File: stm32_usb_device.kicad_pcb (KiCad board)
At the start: 2 copper layers, 0 parts

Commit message: schematic: Add power supply, decoupling caps, pin headers
Signed-off-by: Tomislav Milkovic <tomislav.milkovic95@gmail.com>
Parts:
- added C1: 10u, Capacitor_SMD:C_0603_1608Metric, F.Cu at (94.2, 91.5)
- added C10: 10u, Capacitor_SMD:C_0603_1608Metric, F.Cu at (105.7, 80.9)
- added C11: 100n, Capacitor_SMD:C_0402_1005Metric, F.Cu at (118.6, 80.8)
- added C12: 100n, Capacitor_SMD:C_0402_1005Metric, F.Cu at (118.6, 94.7)
- added C2: 10u, Capacitor_SMD:C_0603_1608Metric, F.Cu at (102.1, 90.3)
- added C3: 10p, Capacitor_SMD:C_0402_1005Metric, F.Cu at (117.7, 88.3)
- added C4: 10p, Capacitor_SMD:C_0402_1005Metric, F.Cu at (117.6, 86.3)
- added C5: 100n, Capacitor_SMD:C_0402_1005Metric, F.Cu at (117.2, 84.1)
- added C6: 100n, Capacitor_SMD:C_0402_1005Metric, F.Cu at (106.1, 82.4)
- added C7: 100n, Capacitor_SMD:C_0402_1005Metric, F.Cu at (116.3, 90.9)
- added C8: 100n, Capacitor_SMD:C_0402_1005Metric, F.Cu at (114.1, 92.8)
- added C9: 100n, Capacitor_SMD:C_0402_1005Metric, F.Cu at (105.8, 91.5)
- added D1: PWR_LED_R, LED_SMD:LED_0603_1608Metric, F.Cu at (100.2, 96.8)
- added D2: USR_LED_R, LED_SMD:LED_0603_1608Metric, F.Cu at (132.0, 81.0)
- added FB1: 100R@100 MHz, Inductor_SMD:L_0805_2012Metric, F.Cu at (91.2, 90.6)
- added J1: USB_A, Connector_USB:USB_A_CNCTech_1001-011-01101_Horizontal, F.Cu at (81.9, 87.5)
- added J2: Conn_01x05, Connector_PinHeader_2.54mm:PinHeader_1x05_P2.54mm_Vertical, F.Cu at (105.4, 97.7)
- added J3: Conn_01x03, Connector_PinHeader_2.54mm:PinHeader_1x03_P2.54mm_Vertical, F.Cu at (107.2, 74.7)
- added R1: 1k5, Resistor_SMD:R_0402_1005Metric, F.Cu at (97.1, 96.7)
- added R2: 1k5, Resistor_SMD:R_0402_1005Metric, F.Cu at (132.0, 84.1)
- added R3: 1k5, Resistor_SMD:R_0402_1005Metric, F.Cu at (111.8, 94.4)
- added R4: 1k5, Resistor_SMD:R_0402_1005Metric, F.Cu at (115.9, 80.2)
- added R5: 1k5, Resistor_SMD:R_0402_1005Metric, F.Cu at (129.4, 78.5)
- added R6: 1k5, Resistor_SMD:R_0402_1005Metric, F.Cu at (94.6, 85.4)
- added R7: 1k5, Resistor_SMD:R_0402_1005Metric, F.Cu at (129.1, 97.3)
- added SW1: RST_SW, Button_Switch_SMD:SW_SPST_CK_RS282G05A3, F.Cu at (124.2, 81.6)
- added SW2: USR_SW, Button_Switch_SMD:SW_SPST_CK_RS282G05A3, F.Cu at (124.2, 94.2)
- added TP1: TestPoint_Small, TestPoint:TestPoint_Pad_D1.0mm, F.Cu at (103.6, 78.3)
- added TP10: TestPoint_Small, TestPoint:TestPoint_Pad_D1.0mm, F.Cu at (103.0, 101.8)
- added TP11: TestPoint_Small, TestPoint:TestPoint_Pad_D1.0mm, F.Cu at (111.0, 102.4)
- added TP12: TestPoint_Small, TestPoint:TestPoint_Pad_D1.0mm, F.Cu at (116.4, 102.7)
- added TP2: TestPoint_Small, TestPoint:TestPoint_Pad_D1.0mm, F.Cu at (112.8, 78.4)
- added TP3: TestPoint_Small, TestPoint:TestPoint_Pad_D1.0mm, F.Cu at (109.6, 78.4)
- added TP4: TestPoint_Small, TestPoint:TestPoint_Pad_D1.0mm, F.Cu at (106.6, 78.4)
- added TP5: TestPoint_Small, TestPoint:TestPoint_Pad_D1.0mm, F.Cu at (96.8, 101.7)
- added TP6: TestPoint_Small, TestPoint:TestPoint_Pad_D1.0mm, F.Cu at (113.7, 102.6)
- added TP7: TestPoint_Small, TestPoint:TestPoint_Pad_D1.0mm, F.Cu at (108.3, 102.2)
- added TP8: TestPoint_Small, TestPoint:TestPoint_Pad_D1.0mm, F.Cu at (99.9, 101.8)
- added TP9: TestPoint_Small, TestPoint:TestPoint_Pad_D1.0mm, F.Cu at (105.8, 102.1)
- added U1: HT7533-1, Package_TO_SOT_SMD:SOT-89-3, F.Cu at (98.6, 90.8)
- added U2: SRV05-4, Package_TO_SOT_SMD:SOT-23-6, F.Cu at (91.1, 87.5)
- added U3: STM32F103C8T6, Package_QFP:LQFP-48_7x7mm_P0.5mm, F.Cu at (110.3, 86.9)
- added Y1: 16M, Crystal:Crystal_SMD_3225-4Pin_3.2x2.5mm, F.Cu at (120.5, 86.8)
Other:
- copper layers 2 -> 4
- rule trace_min: 0.2 -> 0.127

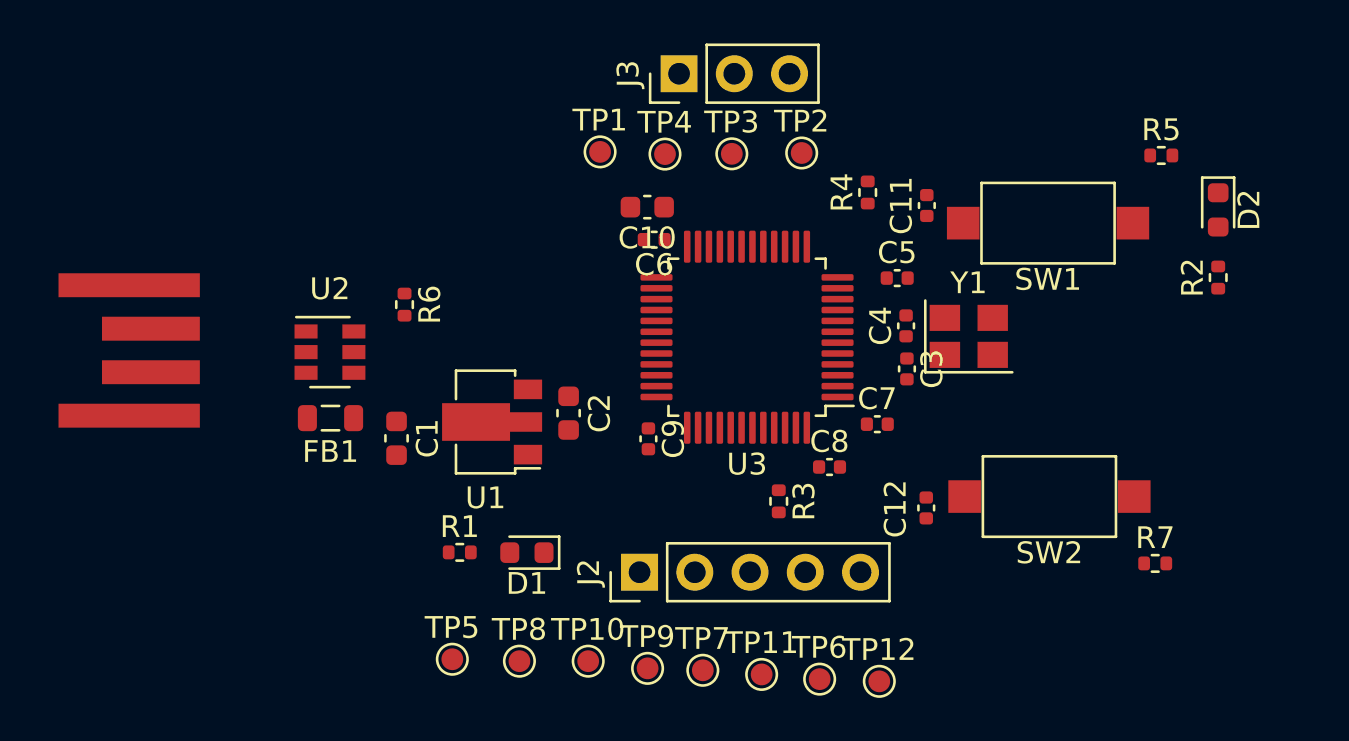
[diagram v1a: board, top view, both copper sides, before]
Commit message: Add USB connector and UART isolators
Make initial PCB layout and routing
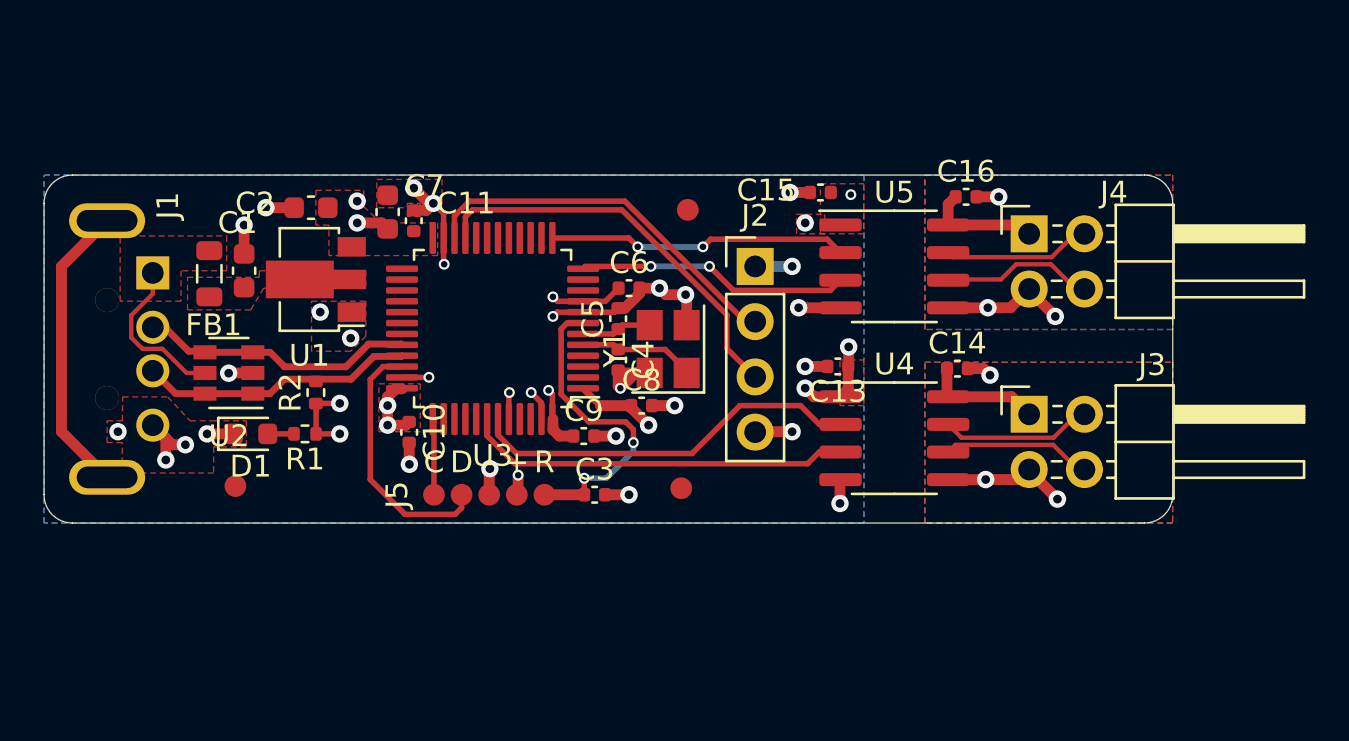
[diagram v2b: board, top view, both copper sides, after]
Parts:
- removed C12: 100n, Capacitor_SMD:C_0402_1005Metric
- removed D2: USR_LED_R, LED_SMD:LED_0603_1608Metric
- removed the R2 at (132.0, 84.1)
- removed R3, R4, R5, R7: 1k5, Resistor_SMD:R_0402_1005Metric
- removed SW1: RST_SW, Button_Switch_SMD:SW_SPST_CK_RS282G05A3
- removed SW2: USR_SW, Button_Switch_SMD:SW_SPST_CK_RS282G05A3
- removed TP1, TP10, TP11, TP12, TP2, TP3, TP4, TP5, TP6, TP7, TP8, TP9: TestPoint_Small, TestPoint:TestPoint_Pad_D1.0mm
- added C13: 100n, Capacitor_SMD:C_0402_1005Metric, F.Cu at (114.5, 88.2)
- added C14: 100n, Capacitor_SMD:C_0402_1005Metric, F.Cu at (120.0, 88.3)
- added C15: 100n, Capacitor_SMD:C_0402_1005Metric, F.Cu at (113.7, 80.2)
- added C16: 100n, Capacitor_SMD:C_0402_1005Metric, F.Cu at (120.4, 80.4)
- added FID1: Fiducial, Fiducial:Fiducial_1mm_Mask2mm, F.Cu at (86.8, 93.7)
- added FID2: Fiducial, Fiducial:Fiducial_1mm_Mask2mm, F.Cu at (107.6, 81.0)
- added FID3: Fiducial, Fiducial:Fiducial_1mm_Mask2mm, F.Cu at (107.3, 93.8)
- added J4: Conn_02x02, Connector_PinHeader_2.54mm:PinHeader_2x02_P2.54mm_Horizontal, F.Cu at (123.3, 82.1)
- added J5: Conn_01x05, Connector_PinHeader_1.27mm:PinHeader_1x05_P1.27mm_Vertical_SMD_Pin1Left, F.Cu at (98.5, 94.1)
- added U4: ADuM1201ARZ, Package_SO:SOIC-8_3.9x4.9mm_P1.27mm, F.Cu at (117.1, 91.5)
- added U5: ADuM1201ARZ, Package_SO:SOIC-8_3.9x4.9mm_P1.27mm, F.Cu at (117.1, 83.6)
- C10: value 10u -> 100n; footprint Capacitor_SMD:C_0603_1608Metric -> Capacitor_SMD:C_0402_1005Metric
- C11: value 100n -> 10u; footprint Capacitor_SMD:C_0402_1005Metric -> Capacitor_SMD:C_0603_1608Metric
- C3: value 10p -> 100n
- C5: value 100n -> 10p
- D1: value PWR_LED_R -> PWR_LED
- J1: footprint Connector_USB:USB_A_CNCTech_1001-011-01101_Horizontal -> USB_A_connector:USB_A_4pin
- J2: value Conn_01x05 -> Conn_01x04; footprint Connector_PinHeader_2.54mm:PinHeader_1x05_P2.54mm_Vertical -> Connector_PinHeader_2.54mm:PinHeader_1x04_P2.54mm_Vertical
- J3: value Conn_01x03 -> Conn_02x02; footprint Connector_PinHeader_2.54mm:PinHeader_1x03_P2.54mm_Vertical -> Connector_PinHeader_2.54mm:PinHeader_2x02_P2.54mm_Horizontal
- moved C11 24.8 mm to (93.8, 81.1)
- moved C7 23.3 mm to (95.0, 81.5), turned to 90 degrees
- moved J3 22.5 mm to (123.3, 90.4), turned to 0 degrees
- moved C3 15.5 mm to (103.3, 94.1), turned to 0 degrees
- moved C2 15.2 mm to (90.3, 80.9), turned to 180 degrees
- moved C10 15.1 mm to (94.8, 91.2), turned to 270 degrees
- moved J2 15.0 mm to (110.7, 83.6), turned to 0 degrees
- moved Y1 13.8 mm to (106.7, 87.4), turned to 90 degrees
- moved D1 13.8 mm to (87.5, 91.3), turned to 0 degrees
- moved C4 13.3 mm to (104.4, 87.9), turned to 270 degrees
- moved C5 13.0 mm to (104.4, 86.0), turned to 90 degrees
- moved U3 11.7 mm to (98.6, 86.5)
- moved U1 10.4 mm to (90.5, 84.2)
- moved C1 10.4 mm to (87.2, 83.8), turned to 90 degrees
- moved C8 9.09 mm to (105.5, 90.0)
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- renumbered R6 to R2
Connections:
- C11 pad 1: /~RESET -> +3V3
- C3 pad 1: /HSE_IN -> /~RESET
- C4 pad 1: /HSE_OUT -> /HSE_IN
- C5 pad 1: +3V3 -> /HSE_OUT
- J1 pad 5: (no net) -> Net-(J1-Pad5)
- J2 pad 2: /~RESET -> /USART3_RX
- J2 pad 3: /JTMS_SWDIO -> /USART3_TX
- J2 pad 4: /JTCK_SWCLK -> GND
- J3 pad 1: /USART3_TX -> /VDD1
- J3 pad 2: /USART3_RX -> /RX1
- J3 pad 3: GND -> GND1
- U3 pad 12: (no net) -> /USART2_TX
- U3 pad 13: (no net) -> /USART2_RX
- U3 pad 2: /USR_LED -> (no net)
- U3 pad 20: /BOOT1 -> (no net)
- U3 pad 3: /USR_SW -> (no net)
- U3 pad 34: /JTMS_SWDIO -> /SWDIO
- U3 pad 37: /JTCK_SWCLK -> /SWCLK
- U3 pad 38: /JTDI -> (no net)
- U3 pad 39: /JTDO_SWO -> (no net)
- U3 pad 40: /~JTRST -> (no net)
- U3 pad 42: (no net) -> /USART1_TX
- U3 pad 43: (no net) -> /USART1_RX
- U3 pad 44: /BOOT0 -> GND
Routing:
- net GND: track 0.00 -> 42.1 mm, vias 0 -> 29
- net +3V3: track 0.00 -> 25.3 mm, vias 0 -> 15
- net /USART3_TX: track 0.00 -> 18.5 mm
- net /USART1_RX: track 0.00 -> 18.1 mm
- net /USART1_TX: track 0.00 -> 17.8 mm
- net /USART3_RX: track 0.00 -> 17.4 mm
- net /~RESET: track 0.00 -> 14.5 mm, vias 0 -> 2
- net /USART2_RX: track 0.00 -> 13.8 mm, vias 0 -> 2
- net Net-(J1-Pad5): track 0.00 -> 13.5 mm
- net /USB_D-: track 0.00 -> 13.1 mm
- net /USB_D+: track 0.00 -> 13.0 mm
- net /USART2_TX: track 0.00 -> 12.5 mm, vias 0 -> 2
- net /SWDIO: track 0.00 -> 11.9 mm
- net +5V: track 0.00 -> 7.45 mm
- net /TX2: track 0.00 -> 7.04 mm
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- added copper zone on B.Cu, net +3V3
- added copper zone on F.Cu, net +3V3
- added copper zone on F.Cu, net +5V
- added copper zone on F.Cu, net /5V_FLT
- added copper zone on F.Cu, net GND
- added copper zone on In1.Cu, net GND
- added copper zone on In2.Cu, net GND
- added copper zone on B.Cu, net GND1
- added copper zone on F.Cu, net GND1
- added copper zone on In1.Cu, net GND1
- added copper zone on In2.Cu, net GND1
- added copper zone on B.Cu, net GND2
- added copper zone on F.Cu, net GND2
- added copper zone on In1.Cu, net GND2
- added copper zone on In2.Cu, net GND2
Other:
- board outline added: 51.9 x 16 mm
- net class Default: clearance 0.2 -> 0.127; trace_width 0.25 -> 0.254
- net class USB added: clearance 0.127, trace_width 0.5, via_dia 0.8, via_drill 0.4
- rule trace_clearance: 0.2 -> 0.127
- rule via_min_drill: 0.3 -> 0.15
- rule via_min_size: 0.4 -> 0.25

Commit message: Finish PCB routing
Signed-off-by: Tomislav Milkovic <tomislav.milkovic95@gmail.com>
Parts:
- removed C13, C14, C15, C16: 100n, Capacitor_SMD:C_0402_1005Metric
- removed the J4 at (123.3, 82.1)
- removed U4, U5: ADuM1201ARZ, Package_SO:SOIC-8_3.9x4.9mm_P1.27mm
- added J1: Conn_01x04, Connector_PinHeader_2.54mm:PinHeader_1x04_P2.54mm_Vertical, F.Cu at (120.2, 83.6)
- added R3: 510R, Resistor_SMD:R_0402_1005Metric, F.Cu at (112.4, 83.4)
- added R4: 510R, Resistor_SMD:R_0402_1005Metric, F.Cu at (112.4, 84.4)
- added R5: 510R, Resistor_SMD:R_0402_1005Metric, F.Cu at (112.4, 86.7)
- added R6: 510R, Resistor_SMD:R_0402_1005Metric, F.Cu at (112.4, 87.7)
- added R7: 510R, Resistor_SMD:R_0402_1005Metric, F.Cu at (112.4, 90.5)
- added R8: 510R, Resistor_SMD:R_0402_1005Metric, F.Cu at (112.4, 91.5)
- J3: value Conn_02x02 -> Conn_01x04; footprint Connector_PinHeader_2.54mm:PinHeader_2x02_P2.54mm_Horizontal -> Connector_PinHeader_2.54mm:PinHeader_1x04_P2.54mm_Vertical
- moved J3 10.7 mm to (115.1, 83.6)
- moved FID1 9.27 mm to (80.0, 87.4)
- moved J2 6.94 mm to (117.6, 83.6)
- moved FID3 3.40 mm to (110.7, 93.8)
- moved FID2 3.10 mm to (110.7, 81.0)
- moved C10 1.71 mm to (93.5, 90.1), turned to 180 degrees
- moved D1 1.20 mm to (87.6, 92.5)
- moved R1 1.20 mm to (90.1, 92.5)
- moved C3 0.42 mm to (102.9, 94.1)
- moved C9 0.30 mm to (102.8, 91.1)
- renumbered J1 to J4
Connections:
- J2 pad 2: /USART3_RX -> Net-(J2-Pad2)
- J2 pad 3: /USART3_TX -> Net-(J2-Pad3)
- J3 pad 1: /VDD1 -> +3V3
- J3 pad 2: /RX1 -> Net-(J3-Pad2)
- J3 pad 3: GND1 -> Net-(J3-Pad3)
- J3 pad 4: /TX1 -> GND
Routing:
- net GND: track 42.1 -> 9.67 mm, vias 29 -> 60
- net Net-(J4-Pad5): track 13.5 -> 0.00 mm
- net +3V3: track 25.3 -> 14.6 mm, vias 15 -> 12
- net Net-(J1-Pad2): track 0.00 -> 10.2 mm
- net Net-(J1-Pad3): track 0.00 -> 9.32 mm
- net Net-(J2-Pad3): track 0.00 -> 7.64 mm
- net /TX2: track 7.04 -> 0.00 mm
- net /RX1: track 6.96 -> 0.00 mm
- net GND1: track 6.96 -> 0.00 mm, vias 3 -> 0
- net /TX1: track 6.87 -> 0.00 mm
- net GND2: track 6.86 -> 0.00 mm, vias 3 -> 0
- net /RX2: track 6.80 -> 0.00 mm
- net Net-(J2-Pad2): track 0.00 -> 6.22 mm
- net /VDD1: track 5.38 -> 0.00 mm
- net /VDD2: track 5.33 -> 0.00 mm
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- added copper zone on B.Cu, net GND
- removed copper zone on B.Cu, net GND1
- removed copper zone on F.Cu, net GND1
- removed copper zone on In1.Cu, net GND1
- removed copper zone on In2.Cu, net GND1
- removed copper zone on B.Cu, net GND2
- removed copper zone on F.Cu, net GND2
- removed copper zone on In1.Cu, net GND2
- removed copper zone on In2.Cu, net GND2
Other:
- board size 51.9 x 16 mm -> 45.5 x 16 mm
- board text added: "1"
- board text added: "2"
- board text added: "3"
- board text added: "3V3"
- board text added: "GND"
- board text added: "JLCJLCJLCJLC"
- board text added: "RX"
- board text added: "Rev 1.0"
- board text added: "TX"
- board text added: "USB to 3x UART"

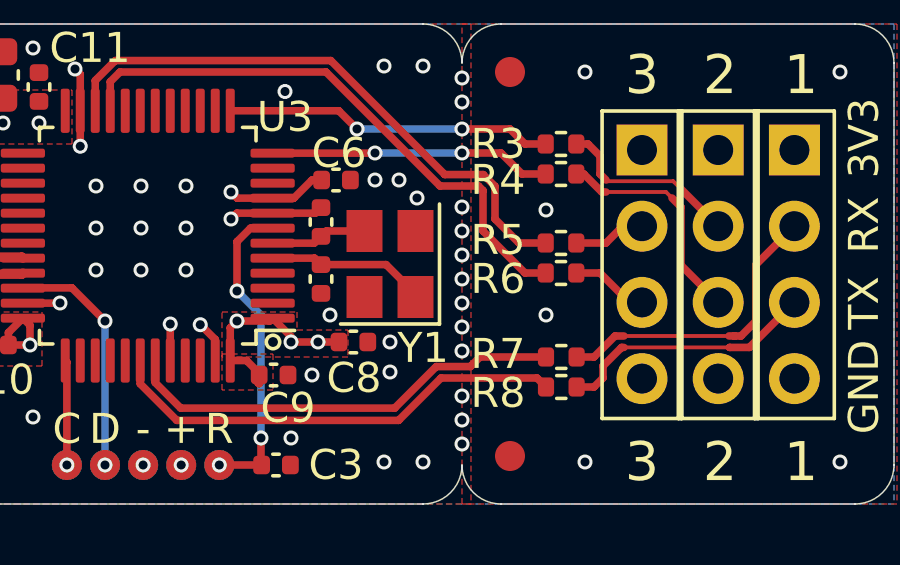
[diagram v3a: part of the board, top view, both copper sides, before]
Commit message: Remove unused net labels
Signed-off-by: Tomislav Milkovic <tomislav.milkovic95@gmail.com>
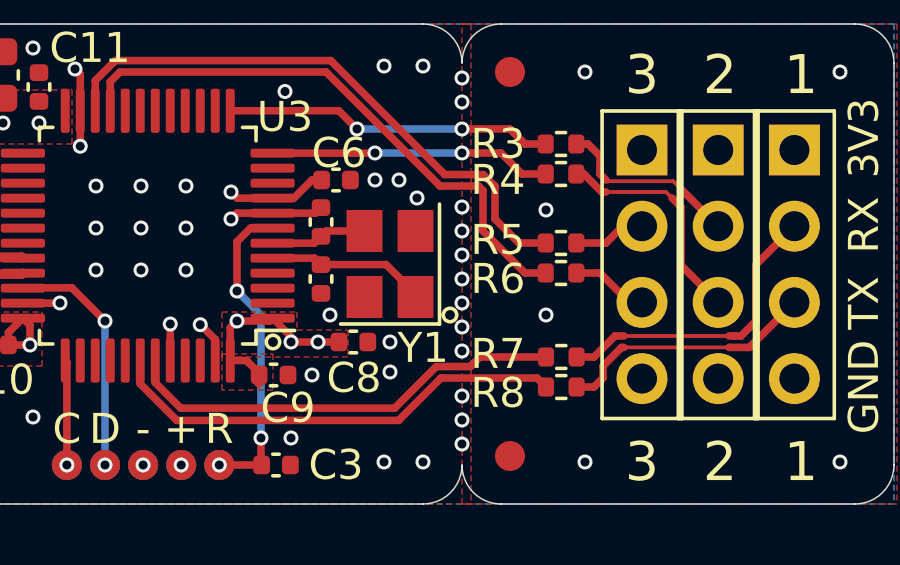
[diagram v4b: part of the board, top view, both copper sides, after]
